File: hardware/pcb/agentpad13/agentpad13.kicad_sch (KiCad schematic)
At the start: 119 parts, among them J1 USB-C, J2 EXPANSION, SW1 MX_Hotswap, SW10 MX_Hotswap, SW11 MX_Hotswap, SW12 MX_Hotswap, SW13 MX_Hotswap, SW14 BOOT, SW15 RESET, SW2 MX_Hotswap, SW3 MX_Hotswap, SW4 MX_Hotswap, SW5 MX_Hotswap, SW6 MX_Hotswap, SW7 MX_Hotswap, SW8 MX_Hotswap, SW9 MX_Hotswap, U1 RP2040, U2 W25Q128JVSIQ, U3 AP2112K-3.3, U4 USBLC6-2SC6, U5 SN74LVC1T45, U6 TTP223, Y1 12MHz ABM8-272-T3

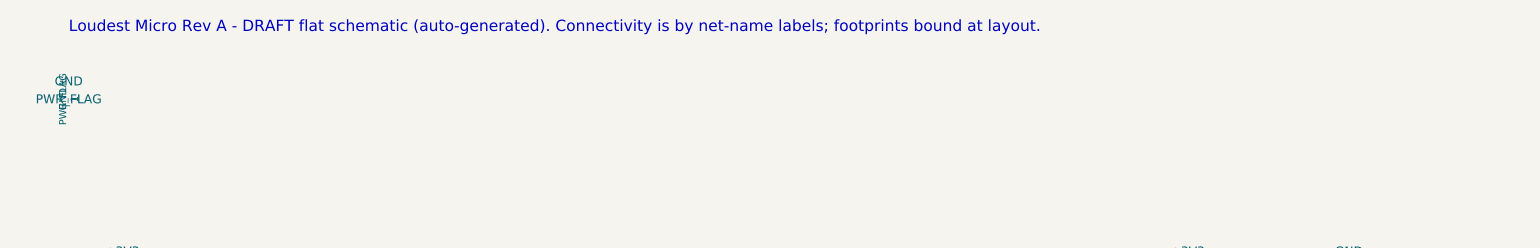
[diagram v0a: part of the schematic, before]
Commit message: Docs: remove legacy product-name references — the project is agentpad13
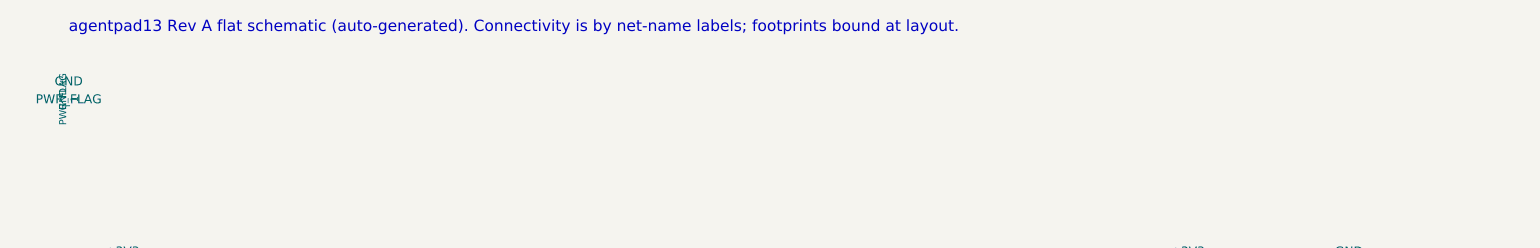
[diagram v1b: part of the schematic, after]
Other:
- note added: "agentpad13 Rev A flat schematic (auto-generated). Connectivity is by net-name labels; footprints bound at layout."
- note removed: "Loudest Micro Rev A - DRAFT flat schematic (auto-generated). Connectivity is by net-name labels; footprints bound at layout."
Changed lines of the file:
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@@
   (symbol (lib_id "power:GND") (at 20.32 20.32 0) (unit 1) (exclude_from_sim no) (in_bom yes) (on_board yes) (dnp no) (property "Reference" "#PWR" (at 20.32 22.86 0) (effects (font (size 1.27 1.27)) (hide yes))) (property "Value" "GND" (at 20.32 17.78 0) (effects (font (size 1.27 1.27)))) (instances (project "loudest-micro" (path "/530b0722-cd32-4468-b548-8efc971bd5b8" (reference "#PWR?") (unit 1)))))
   (symbol (lib_id "power:PWR_FLAG") (at 20.32 20.32 0) (unit 1) (exclude_from_sim no) (in_bom yes) (on_board yes) (dnp no) (property "Reference" "#FLG" (at 20.32 22.86 0) (effects (font (size 1.27 1.27)) (hide yes))) (property "Value" "PWR_FLAG" (at 20.32 20.32 0) (effects (font (size 1.27 1.27)))) (instances (project "loudest-micro" (path "/530b0722-cd32-4468-b548-8efc971bd5b8" (reference "#FLG?") (unit 1)))))
-  (text "Loudest Micro Rev A - DRAFT flat schematic (auto-generated). Connectivity is by net-name labels; footprints bound at layout." (at 20.32 10.16 0) (effects (font (size 1.6 1.6)) (justify left)))
+  (text "agentpad13 Rev A flat schematic (auto-generated). Connectivity is by net-name labels; footprints bound at layout." (at 20.32 10.16 0) (effects (font (size 1.6 1.6)) (justify left)))
   (sheet_instances (path "/" (page "1")))
 )

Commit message: BOM: SW14/SW15 tact was the wrong part for its footprint (PCBWay catch)
The BOOT/RESET tact switches were specified as XKB TS-1187A (LCSC C318884)
against the footprint SW_SPST_PTS645Sx43SMTR92 — a C&K PTS645 6.0 x 6.0 mm /
H4.3 gull-wing land pattern. The TS-1187A is a 5.1 x 5.1 mm part with a 6.5 mm
lead span against this footprint's 7.96 mm pad span: its leads land ~45 um over
the pad edge (~9 % of pad area). Not solderable. PCBWay's component
verification caught it during the order review.

Corrected part (land-pattern verified to 0.01 mm X / 0.00 mm Y):

  C&K PTS645SM43SMTR92 LFS — LCSC C221880, DigiKey CKN9112CT-ND
  6.0 x 6.0 mm SMT gull-wing, H4.3, 160 gf, SPST-NO, ~$0.313@10

Drop-in alternates on the identical land pattern:
  Omron B3S-1000P            (LCSC C180420, 160 gf)
  Megastar ZX-QC66-4.3TP     (LCSC C7470150, 260 gf)
  C&K PTS645SK43SMTR92 LFS   (DigiKey CKN9084CT-ND, 260 gf — stiffer, deeper stock)

DO NOT SUBSTITUTE: C&K PTS645SM43JSMTR92 LFS (LCSC C2801847). One inserted
letter, J-lead version, different land pattern.

Cost impact: $0.018 -> $0.313 each = +$0.59/board for the pair.

Changed:
  hardware/pcb/BOM.csv                          SW14/SW15 row: MPN, manufacturer,
                                                LCSC, DigiKey, price, alternates, notes
  hardware/pcb/assembly/bom_opaque.csv          regenerated by build_fabpack.py
  hardware/pcb/assembly/bom_translucent.csv     regenerated by build_fabpack.py
  hardware/pcb/assembly/hand_solder_afterlist.csv  regenerated (it duplicated the MPN)
  hardware/pcb/fabpack_{opaque,translucent}.zip those three members replaced in place
  hardware/pcb/agentpad13/agentpad13.kicad_sch  SW14/SW15 MPN + LCSC symbol properties

The bare board did not change. Every Gerber, drill file, drill map, both CPLs
and gerbers.zip are byte-identical; inside the two fabpack zips all 14 other
members keep their original CRC32. The schematic edit touches only the MPN and
LCSC property strings — netlist export bef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
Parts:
- SW14, SW15: LCSC C318884 -> C221880; MPN TS-1187A -> PTS645SM43SMTR92 LFS
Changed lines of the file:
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@@
   (wire (pts (xy 346.71 101.6) (xy 351.79 101.6)) (stroke (width 0) (type default)))
   (global_label "BOOTSEL" (shape input) (at 351.79 101.6 0) (effects (font (size 1.27 1.27)) (justify left)))
-  (symbol (lib_id "Switch:SW_Push") (at 340.36 125.73 0) (unit 1) (exclude_from_sim no) (in_bom yes) (on_board yes) (dnp no) (property "Reference" "SW14" (at 350.52 124.46 0) (effects (font (size 1.27 1.27)))) (property "Value" "BOOT" (at 350.52 127 0) (effects (font (size 1.27 1.27)))) (property "Footprint" "Button_Switch_SMD:SW_SPST_PTS645Sx43SMTR92" (at 340.36 125.73 0) (effects (font (size 1.27 1.27)) (hide yes))) (property "Datasheet" "~" (at 340.36 125.73 0) (effects (font (size 1.27 1.27)) (hide yes))) (property "Description" "BOOTSEL tact" (at 340.36 125.73 0) (effects (font (size 1.27 1.27)) (hide yes))) (property "MPN" "TS-1187A" (at 340.36 125.73 0) (effects (font (size 1.27 1.27)) (hide yes))) (property "LCSC" "C318884" (at 340.36 125.73 0) (effects (font (size 1.27 1.27)) (hide yes))) (property "JLC" "Basic" (at 340.36 125.73 0) (effects (font (size 1.27 1.27)) (hide yes))) (pin "1") (pin "2") (instances (project "loudest-micro" (path "/530b0722-cd32-4468-b548-8efc971bd5b8" (reference "SW14") (unit 1)))))
+  (symbol (lib_id "Switch:SW_Push") (at 340.36 125.73 0) (unit 1) (exclude_from_sim no) (in_bom yes) (on_board yes) (dnp no) (property "Reference" "SW14" (at 350.52 124.46 0) (effects (font (size 1.27 1.27)))) (property "Value" "BOOT" (at 350.52 127 0) (effects (font (size 1.27 1.27)))) (property "Footprint" "Button_Switch_SMD:SW_SPST_PTS645Sx43SMTR92" (at 340.36 125.73 0) (effects (font (size 1.27 1.27)) (hide yes))) (property "Datasheet" "~" (at 340.36 125.73 0) (effects (font (size 1.27 1.27)) (hide yes))) (property "Description" "BOOTSEL tact" (at 340.36 125.73 0) (effects (font (size 1.27 1.27)) (hide yes))) (property "MPN" "PTS645SM43SMTR92 LFS" (at 340.36 125.73 0) (effects (font (size 1.27 1.27)) (hide yes))) (property "LCSC" "C221880" (at 340.36 125.73 0) (effects (font (size 1.27 1.27)) (hide yes))) (property "JLC" "Basic" (at 340.36 125.73 0) (effects (font (size 1.27 1.27)) (hide yes))) (pin "1") (pin "2") (instances (project "loudest-micro" (path "/530b0722-cd32-4468-b548-8efc971bd5b8" (reference "SW14") (unit 1)))))
   (wire (pts (xy 334.01 125.73) (xy 328.93 125.73)) (stroke (width 0) (type default)))
   (global_label "BOOTSEL" (shape input) (at 328.93 125.73 180) (effects (font (size 1.27 1.27)) (justify right)))
@@
   (wire (pts (xy 646.43 44.45) (xy 651.51 44.45)) (stroke (width 0) (type default)))
   (global_label "RUN" (shape input) (at 651.51 44.45 0) (effects (font (size 1.27 1.27)) (justify left)))
-  (symbol (lib_id "Switch:SW_Push") (at 640.08 69.85 0) (unit 1) (exclude_from_sim no) (in_bom yes) (on_board yes) (dnp no) (property "Reference" "SW15" (at 650.24 68.58 0) (effects (font (size 1.27 1.27)))) (property "Value" "RESET" (at 650.24 71.12 0) (effects (font (size 1.27 1.27)))) (property "Footprint" "Button_Switch_SMD:SW_SPST_PTS645Sx43SMTR92" (at 640.08 69.85 0) (effects (font (size 1.27 1.27)) (hide yes))) (property "Datasheet" "~" (at 640.08 69.85 0) (effects (font (size 1.27 1.27)) (hide yes))) (property "Description" "RESET tact" (at 640.08 69.85 0) (effects (font (size 1.27 1.27)) (hide yes))) (property "MPN" "TS-1187A" (at 640.08 69.85 0) (effects (font (size 1.27 1.27)) (hide yes))) (property "LCSC" "C318884" (at 640.08 69.85 0) (effects (font (size 1.27 1.27)) (hide yes))) (property "JLC" "Basic" (at 640.08 69.85 0) (effects (font (size 1.27 1.27)) (hide yes))) (pin "1") (pin "2") (instances (project "loudest-micro" (path "/530b0722-cd32-4468-b548-8efc971bd5b8" (reference "SW15") (unit 1)))))
+  (symbol (lib_id "Switch:SW_Push") (at 640.08 69.85 0) (unit 1) (exclude_from_sim no) (in_bom yes) (on_board yes) (dnp no) (property "Reference" "SW15" (at 650.24 68.58 0) (effects (font (size 1.27 1.27)))) (property "Value" "RESET" (at 650.24 71.12 0) (effects (font (size 1.27 1.27)))) (property "Footprint" "Button_Switch_SMD:SW_SPST_PTS645Sx43SMTR92" (at 640.08 69.85 0) (effects (font (size 1.27 1.27)) (hide yes))) (property "Datasheet" "~" (at 640.08 69.85 0) (effects (font (size 1.27 1.27)) (hide yes))) (property "Description" "RESET tact" (at 640.08 69.85 0) (effects (font (size 1.27 1.27)) (hide yes))) (property "MPN" "PTS645SM43SMTR92 LFS" (at 640.08 69.85 0) (effects (font (size 1.27 1.27)) (hide yes))) (property "LCSC" "C221880" (at 640.08 69.85 0) (effects (font (size 1.27 1.27)) (hide yes))) (property "JLC" "Basic" (at 640.08 69.85 0) (effects (font (size 1.27 1.27)) (hide yes))) (pin "1") (pin "2") (instances (project "loudest-micro" (path "/530b0722-cd32-4468-b548-8efc971bd5b8" (reference "SW15") (unit 1)))))
   (wire (pts (xy 633.73 69.85) (xy 628.65 69.85)) (stroke (width 0) (type default)))
   (global_label "RUN" (shape input) (at 628.65 69.85 180) (effects (font (size 1.27 1.27)) (justify right)))

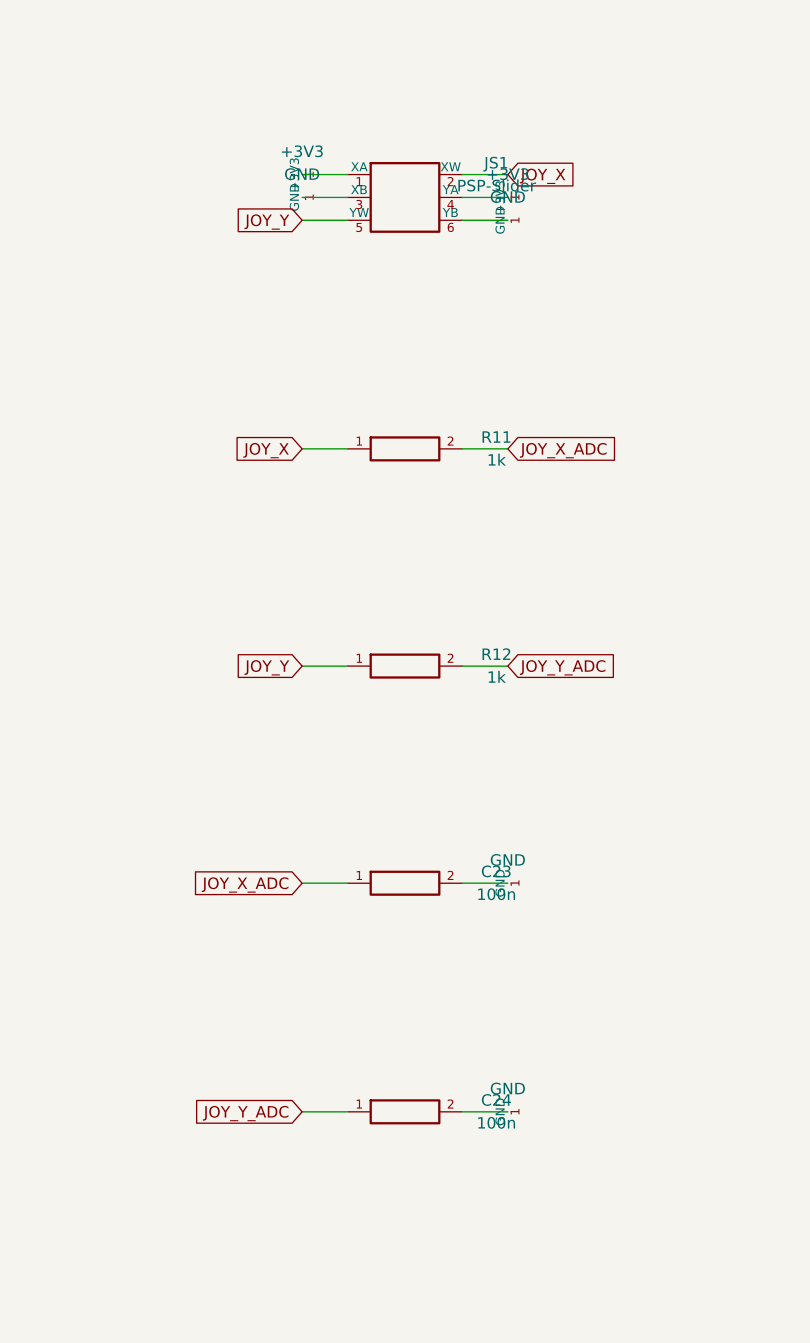
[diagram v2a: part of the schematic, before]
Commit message: JS1: public mirror was carrying the dead Adafruit 3103; re-sync to the YA13
The 2026-07-19 joystick reversal (Adafruit 3103 PSP-slider -> YTL
YA13-FL7.4-B5Ka(45-10)-R-Y06, LCSC C37323742, machine-placed THT) landed in
the private source but not here, so this repo had become the one telling
readers to buy and meter a part that is no longer used.

- hardware/pcb/agentpad13/agentpad13.kicad_sch: re-snapshotted from the
  corrected private schematic, re-applying only the 2 branding hunks
  (title_block, descriptive text). Diff vs private is back to exactly those
  2 hunks / 4 lines -- it was 5 hunks before this commit. JS1 is now
  Joystick:YA13_Tilt_Gimbal with MP1-MP4 GND frame lugs declared.
- hardware/pcb/lib/Joystick.pretty/YA13-FL7.4-B5Ka_C37323742.kicad_mod: NEW.
  Exported from the routed board v5_6.kicad_pcb (board itself untouched).
  10 pads verified identical to the board's JS1: 6 signal Ø1.0 drill / Ø1.8
  pad + 4 lug Ø1.2 drill / Ø2.0 pad, matching the frozen hole table.
- hardware/pcb/agentpad13/fp-lib-table: register the Joystick lib. This
  clears the ERC warning "does not include the footprint library 'Joystick'"
  (342 -> 341 violations, 0 error-severity maintained; the remaining 341 are
  the documented headless lib_symbol_issues noise). The superseded
  loudest.pretty row is annotated, not removed.
- firmware/FIRMWARE-V4-NOTES.md, firmware/loudest_micro/keyboard.json,
  firmware/loudest_micro/config.h: the "meter the Adafruit 3103's pinout
  before soldering" instruction is struck and corrected. Nothing to buy,
  nothing to meter, nothing to hand-solder -- JS1 is fab-placed. The only
  residual first-power-on item is the axis-direction polarity note
  (firmware/POLARITY-NOTE.md), a one-line config flip per reversed axis.

Superseded footprint lib/loudest.pretty/JS1_PSP_slider_4pad_handsolder.kicad_mod
is deliberately RETAINED as the record of what was replaced; verified
referenced by no live file.

Order-facing files (BOM.csv, assembly/bom_*.csv, as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
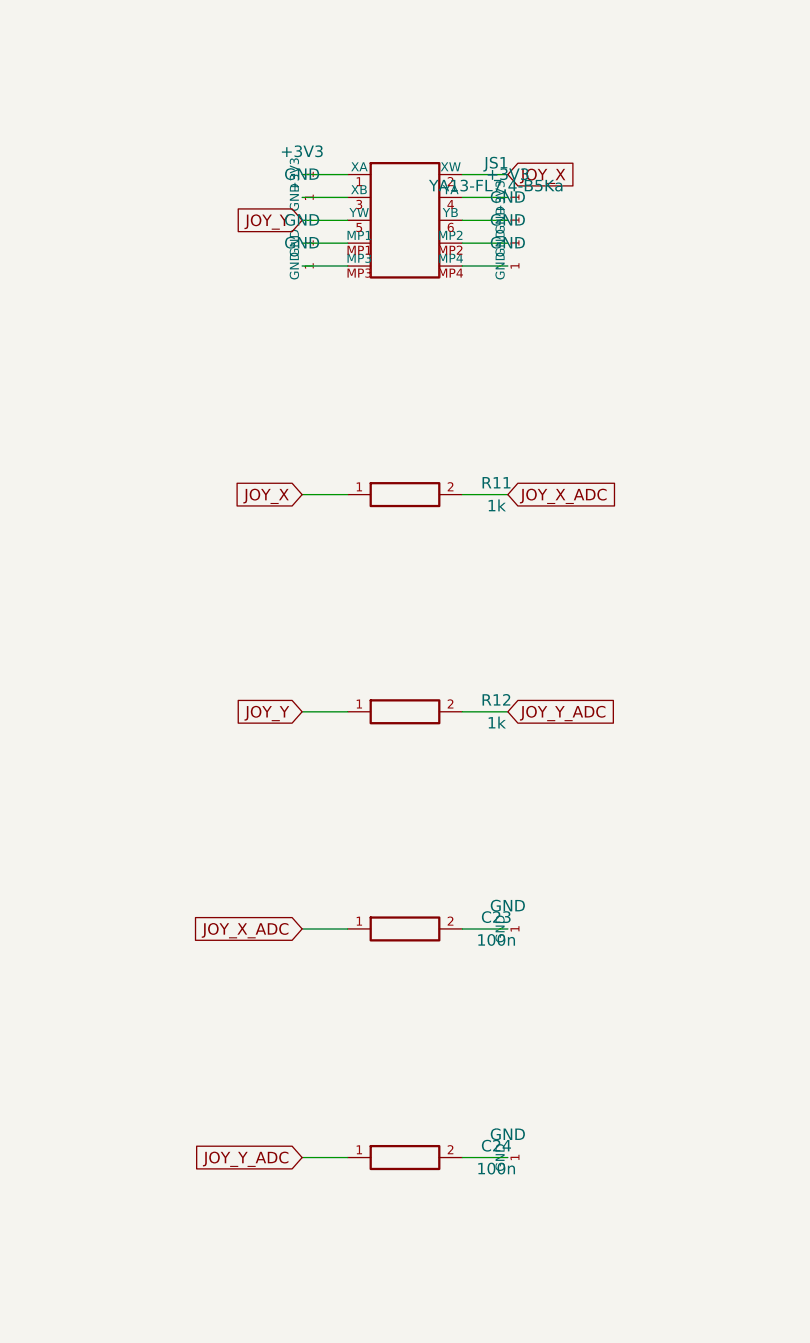
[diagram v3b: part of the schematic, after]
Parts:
- JS1: value PSP-Slider -> YA13-FL7.4-B5Ka; footprint loudest:JS1_PSP_slider_4pad_handsolder -> Joystick:YA13-FL7.4-B5Ka_C37323742; symbol Joystick:PSP_Slider -> Joystick:YA13_Tilt_Gimbal; JLC n/a(hand-solder) -> PCBWay-THT; LCSC (none) -> C37323742; MPN Adafruit 3103 (PSP-3000); fallback 444/PSP clone -> YA13-FL7.4-B5Ka(45-10)-R-Y06
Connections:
- net GND: now also JS1.MP1, JS1.MP2, JS1.MP3, JS1.MP4
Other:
- moved on the sheet: C23, C24, R11, R12
